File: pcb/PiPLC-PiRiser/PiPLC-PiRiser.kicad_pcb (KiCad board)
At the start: 2 copper layers, 51.9 x 29.6 mm, 2 parts, among them J1 Male, J2 Female

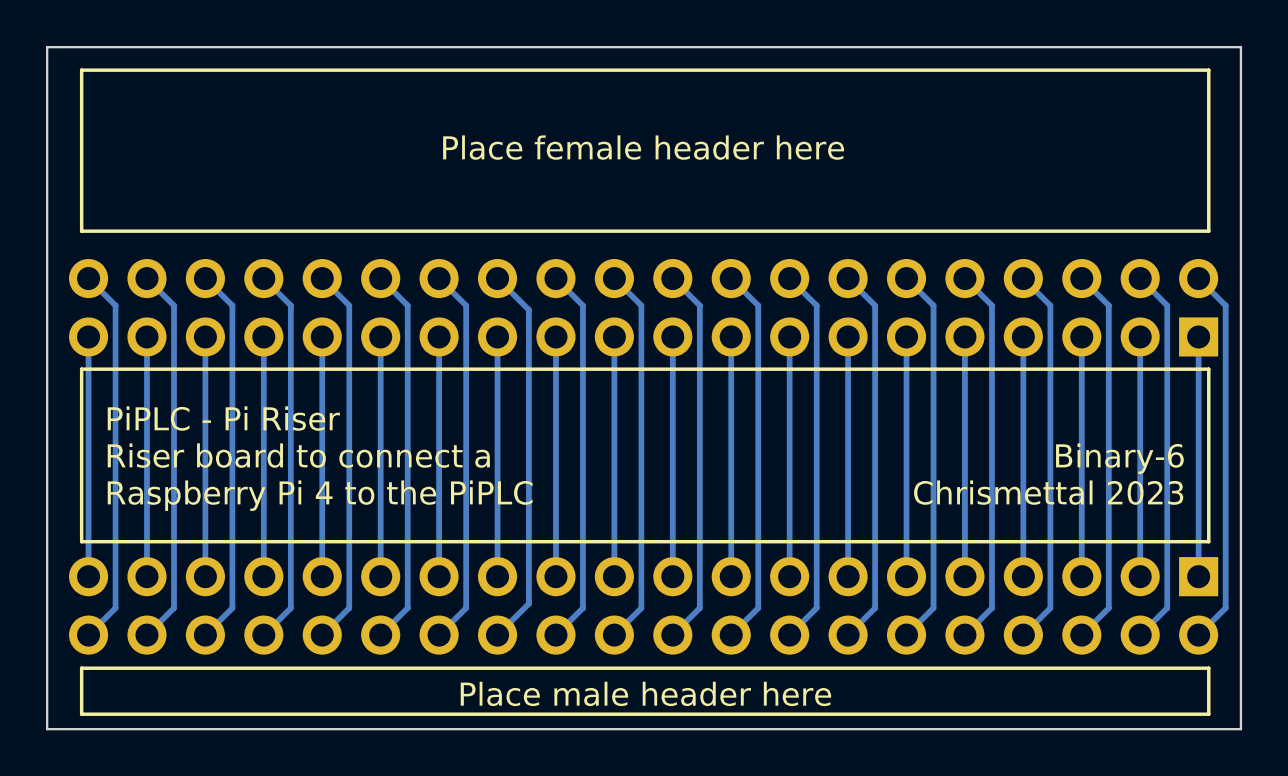
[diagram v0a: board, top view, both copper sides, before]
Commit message: [PiRiser] Double up routing
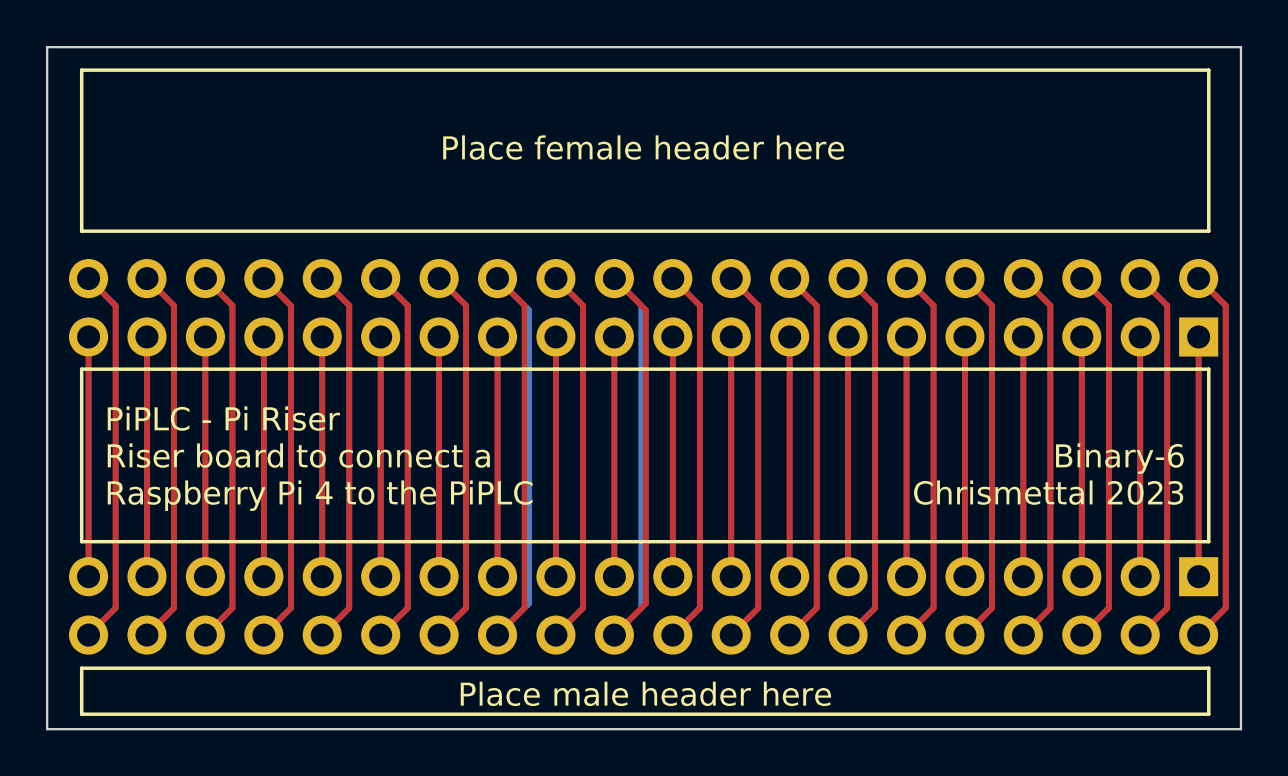
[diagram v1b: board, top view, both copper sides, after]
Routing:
- net Net-(J1-Pin_22): track 16.5 -> 33.1 mm
- net Net-(J1-Pin_8): track 16.5 -> 32.9 mm
- net Net-(J1-Pin_4): track 16.5 -> 32.9 mm
- net Net-(J1-Pin_28): track 16.5 -> 32.9 mm
- net Net-(J1-Pin_24): track 16.5 -> 32.9 mm
- net Net-(J1-Pin_2): track 16.5 -> 32.9 mm
- net Net-(J1-Pin_18): track 16.5 -> 32.9 mm
- net Net-(J1-Pin_16): track 16.5 -> 32.9 mm
- net Net-(J1-Pin_12): track 16.5 -> 32.9 mm
- net Net-(J1-Pin_10): track 16.5 -> 32.9 mm
- net Net-(J1-Pin_40): track 16.5 -> 32.9 mm
- net Net-(J1-Pin_38): track 16.5 -> 32.9 mm
- net Net-(J1-Pin_36): track 16.5 -> 32.9 mm
- net Net-(J1-Pin_34): track 16.5 -> 32.9 mm
- net Net-(J1-Pin_32): track 16.5 -> 32.9 mm
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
